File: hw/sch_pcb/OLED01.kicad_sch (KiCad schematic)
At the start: 45 parts, among them J1 Conn_01x04_Male, J2 HEADER_2x03_PARALLEL, J3 HEADER_2x03_PARALLEL, J4 HEADER_2x03_PARALLEL, J5 HEADER_1x03, J6 HEADER_2x05_PARALLEL, U1 TLV840, U2 MIC5504-2.5YM5, U3 MAX5026, U4 TSC2007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

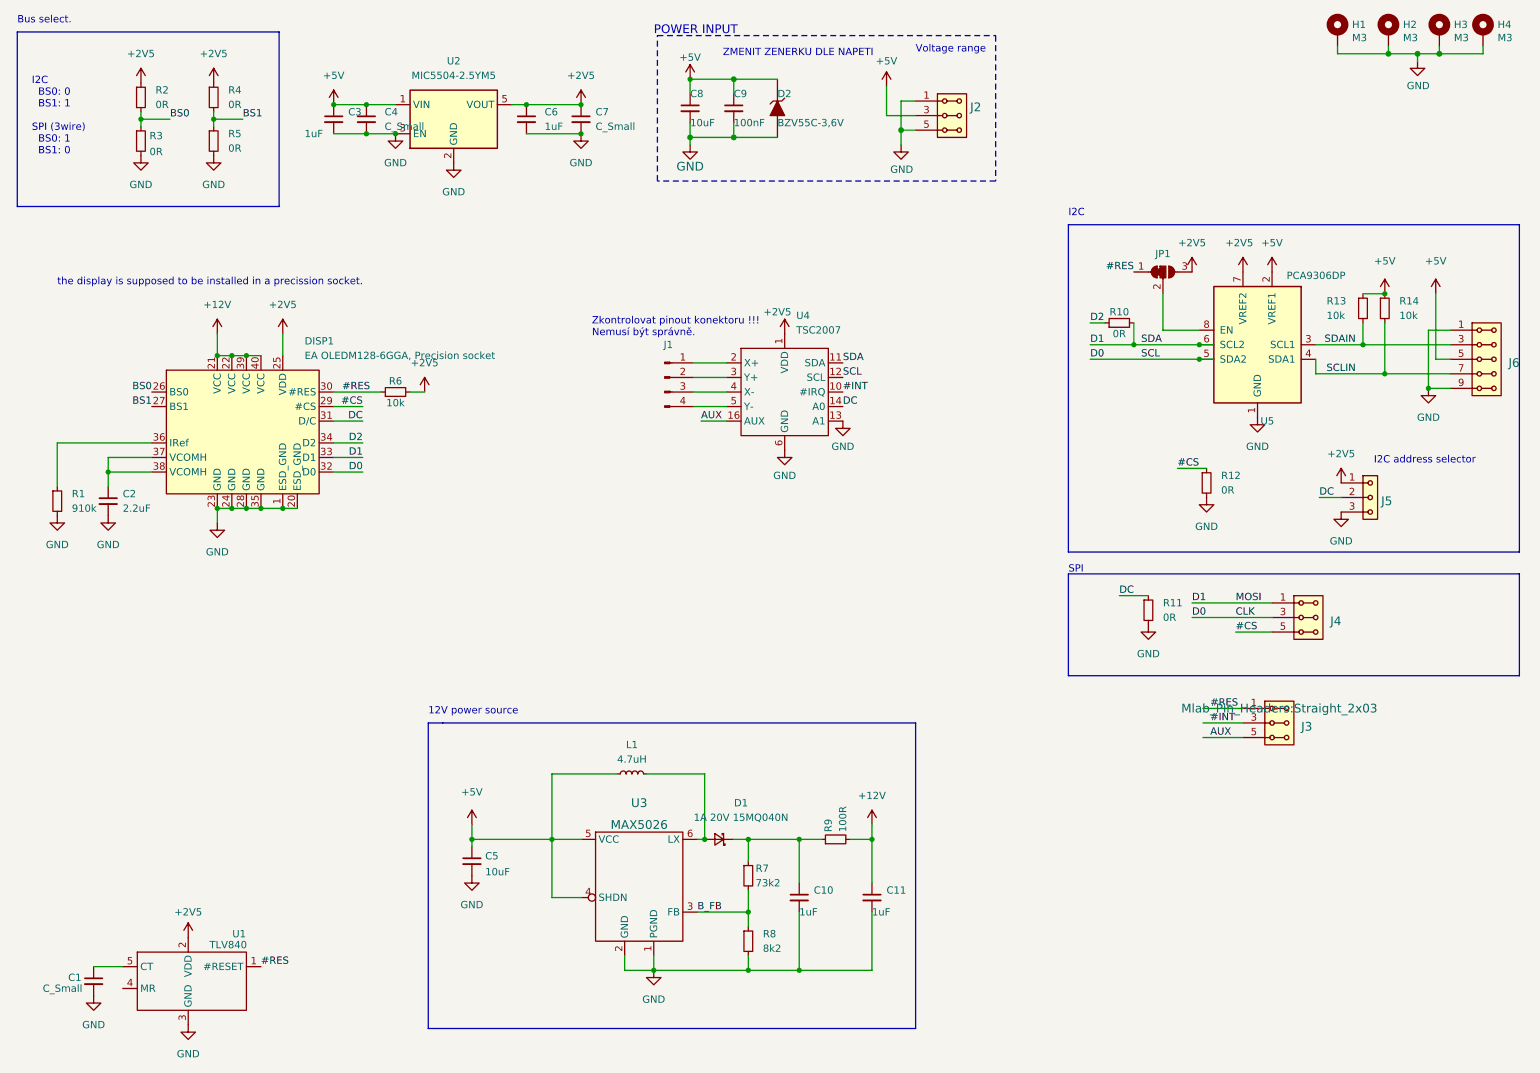
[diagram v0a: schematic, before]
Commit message: Update schematics, add reset circuit, route pcb
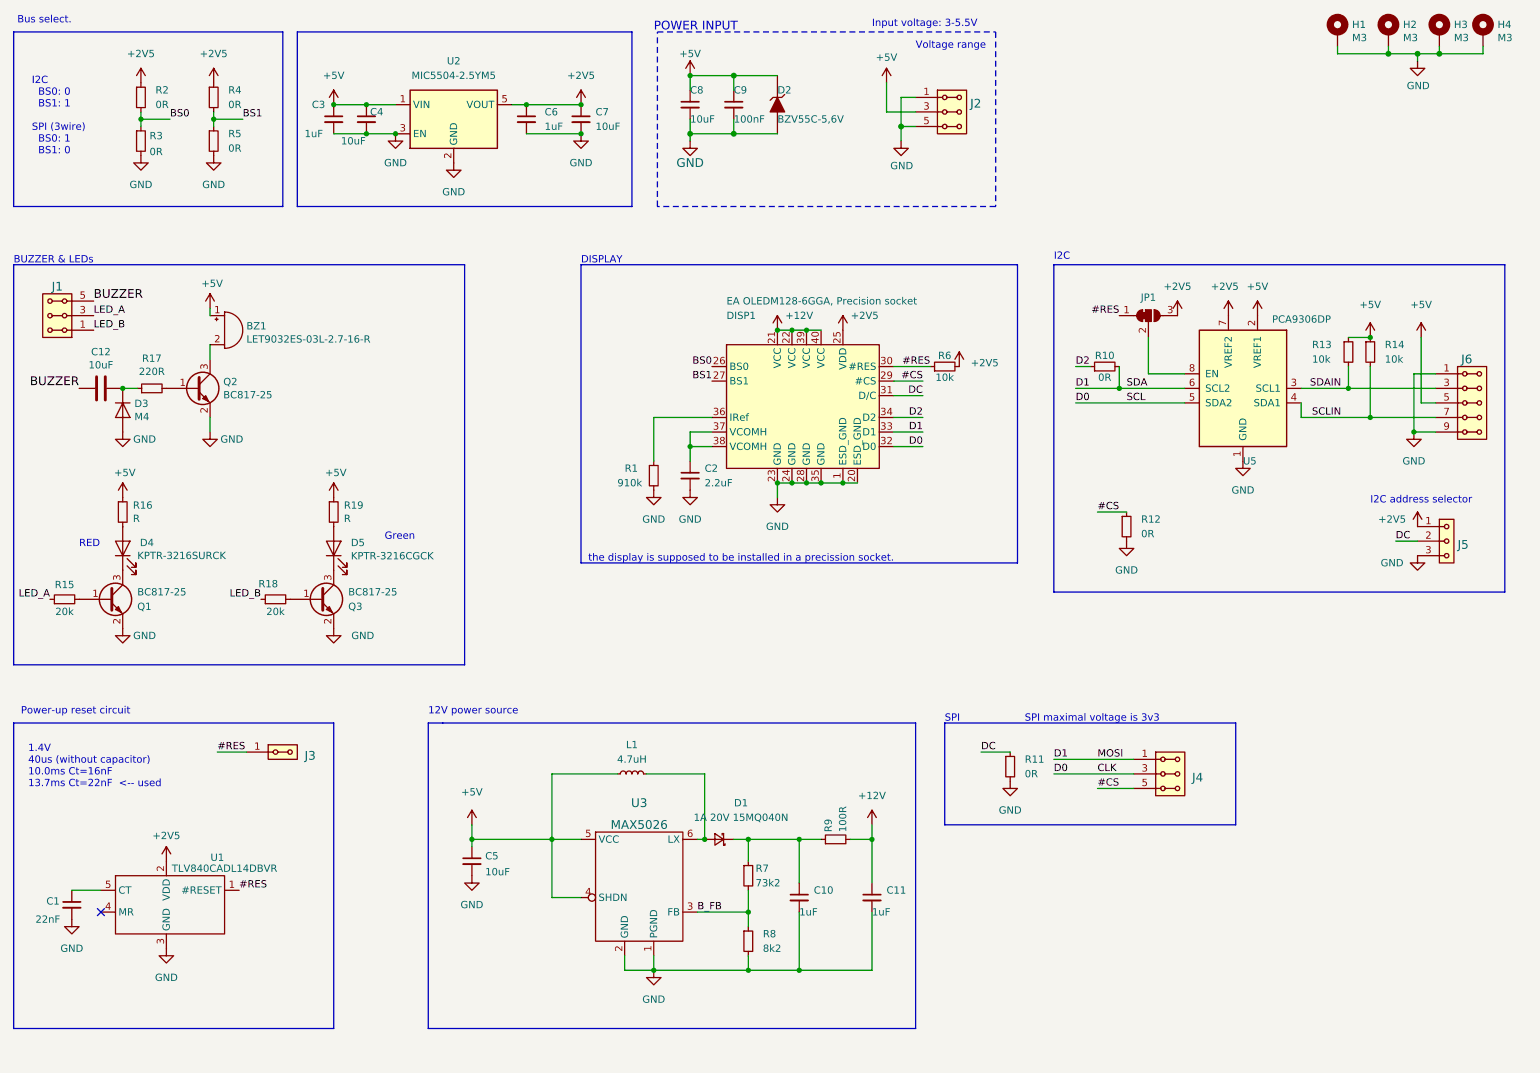
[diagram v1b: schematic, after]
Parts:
- removed J1: Conn_01x04_Male, Connector_FFC-FPC:TE_84952-4_1x04-1MP_P1.0mm_Horizontal, symbol Connector:Conn_01x04_Male
- removed U4: TSC2007, Package_SO:TSSOP-16_4.4x5mm_P0.65mm, symbol MLAB_IO:TSC2007
- added BZ1: LET9032ES-03L-2.7-16-R, MLAB_BUZZER:MagneticBuzzer_LET9032ES-03L-2.7-16-R, symbol Device:Buzzer
- added C12: 10uF, Resistor_SMD:R_0805_2012Metric, symbol Device:C
- added D3: M4, Diode_SMD:D_SMA, symbol Device:D
- added D4: KPTR-3216SURCK, Mlab_D:LED_1206_2, symbol Device:LED
- added D5: KPTR-3216CGCK, Mlab_D:LED_1206_2, symbol Device:LED
- added J1: HEADER_2x03_PARALLEL, Mlab_Pin_Headers:Straight_2x03, symbol MLAB_HEADER:HEADER_2x03_PARALLEL
- added Q1, Q2, Q3: BC817-25, Package_TO_SOT_SMD:SOT-23, symbol Device:Q_NPN_BEC
- added R15, R18: 20k, Resistor_SMD:R_0805_2012Metric, symbol Device:R_Small
- added R16, R19: R, Resistor_SMD:R_0805_2012Metric, symbol Device:R_Small
- added R17: 220R, Resistor_SMD:R_0805_2012Metric, symbol Device:R_Small
- C1: UST_ID (none) -> 5c70984712875079b91f8b4a
- D2: value BZV55C-3,6V -> BZV55C-5,6V; UST_ID (none) -> 5c70984512875079b91f88b2
- J3: value HEADER_2x03_PARALLEL -> HEADER_2x01_PARALLEL; footprint Mlab_Pin_Headers:Straight_2x03 -> Mlab_Pin_Headers:Straight_2x01; symbol MLAB_HEADER:HEADER_2x03_PARALLEL -> MLAB_HEADER:HEADER_2x01_PARALLEL
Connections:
- net +5V: now also BZ1.1 (-), R16.1, R19.1
- net GND: now also D3.2 (A), Q1.2 (E), Q2.2 (E), Q3.2 (E)
- removed net #INT: J3.3, J3.4
- removed net AUX: J3.5, J3.6
- new net: D5.2 (A), R19.2
- new net: C12.2, D3.1 (K), R17.1
- new net: D4.1 (K), Q1.3 (C)
- new net: D4.2 (A), R16.2
- new net: Q1.1 (B), R15.2
- new net: Q3.1 (B), R18.2
- new net: D5.1 (K), Q3.3 (C)
- new net: Q2.1 (B), R17.2
- new net: BZ1.2 (+), Q2.3 (C)
- new net BUZZER: C12.1, J1.5, J1.6
- new net LED_A: J1.3, J1.4, R15.1
- new net LED_B: J1.1, J1.2, R18.1
- no-connect marks 0 -> 1
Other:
- note added: "1.4V 40us (without capacitor) 10.0ms Ct=16nF 13.7ms Ct=22nF <-- used"
- note added: "BUZZER & LEDs"
- note added: "DISPLAY"
- note added: "Green"
- note added: "Input voltage: 3-5.5V"
- note added: "Power-up reset circuit"
- note added: "RED"
- note added: "SPI maximal voltage is 3v3"
- note removed: "ZMENIT ZENERKU DLE NAPETI"
- note removed: "Zkontrolovat pinout konektoru !!! Nemusí být správně."
- moved on the sheet: C1, C2, C8, C9, D2, DISP1, J2, J4, J5, J6, JP1, R1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

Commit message: update assets
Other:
- note added: "Or CMI-9653S-SMT-TR with integrated driver (replace C12 with jumper, remove D3)"
- moved on the sheet: L1
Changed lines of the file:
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@@
     (stroke (width 0) (type default) (color 0 0 0 0))
   )
-  (wire (pts (xy 139.7 148.59) (xy 139.7 160.02))
+  (wire (pts (xy 139.7 151.13) (xy 139.7 160.02))
     (stroke (width 0) (type default) (color 0 0 0 0))
   )
@@
     (stroke (width 0) (type default) (color 0 0 0 0))
   )
-  (wire (pts (xy 129.54 148.59) (xy 139.7 148.59))
+  (wire (pts (xy 129.54 151.13) (xy 139.7 151.13))
     (stroke (width 0) (type default) (color 0 0 0 0))
   )
@@
     (stroke (width 0) (type solid) (color 0 0 0 0))
   )
-  (wire (pts (xy 124.46 148.59) (xy 113.03 148.59))
+  (wire (pts (xy 124.46 151.13) (xy 113.03 151.13))
     (stroke (width 0) (type default) (color 0 0 0 0))
   )
@@
     (stroke (width 0) (type default) (color 0 0 0 0))
   )
-  (wire (pts (xy 113.03 148.59) (xy 113.03 160.02))
+  (wire (pts (xy 113.03 151.13) (xy 113.03 160.02))
     (stroke (width 0) (type default) (color 0 0 0 0))
   )
@@
   )
   (text "12V power source" (at 91.44 138.43 0)
+    (effects (font (size 1.27 1.27)) (justify left bottom))
+  )
+  (text "Or CMI-9653S-SMT-TR\nwith integrated driver\n(replace C12 with jumper, remove D3)"
+    (at 59.69 67.31 0)
     (effects (font (size 1.27 1.27)) (justify left bottom))
   )
@@
     (pin "1")
   )
-  (symbol (lib_id "Device:L_Small") (at 127 148.59 90) (unit 1)
-    (in_bom yes) (on_board yes) (fields_autoplaced)
-    (property "Reference" "L1" (id 0) (at 127 143.51 90))
-    (property "Value" "4.7uH" (id 1) (at 127 146.05 90))
-    (property "Footprint" "Inductor_SMD:L_Bourns_SRN6045TA" (id 2) (at 127 148.59 0)
-      (effects (font (size 1.27 1.27)) hide)
-    )
-    (property "Datasheet" "" (id 3) (at 127 148.59 0)
-      (effects (font (size 1.27 1.27)) hide)
-    )
-    (property "Datasheet" "~" (id 4) (at 127 148.59 0)
-      (effects (font (size 1.27 1.27)) hide)
-    )
-    (property "UST_ID" "5c70984412875079b91f8828" (id 6) (at 127 148.59 90)
+  (symbol (lib_id "Device:L_Small") (at 127 151.13 90) (unit 1)
+    (in_bom yes) (on_board yes) (fields_autoplaced)
+    (property "Reference" "L1" (id 0) (at 127 146.05 90))
+    (property "Value" "4.7uH" (id 1) (at 127 148.59 90))
+    (property "Footprint" "Inductor_SMD:L_Bourns_SRN6045TA" (id 2) (at 127 151.13 0)
+      (effects (font (size 1.27 1.27)) hide)
+    )
+    (property "Datasheet" "" (id 3) (at 127 151.13 0)
+      (effects (font (size 1.27 1.27)) hide)
+    )
+    (property "Datasheet" "~" (id 4) (at 127 151.13 0)
+      (effects (font (size 1.27 1.27)) hide)
+    )
+    (property "UST_ID" "5c70984412875079b91f8828" (id 6) (at 127 151.13 90)
       (effects (font (size 1.27 1.27)) hide)
     )
@@
   )
   (symbol (lib_id "MLAB_IO:MAX5026") (at 128.27 167.64 0) (unit 1)
-    (in_bom yes) (on_board yes) (fields_autoplaced)
-    (property "Reference" "U3" (id 0) (at 128.27 153.67 0)
+    (in_bom yes) (on_board yes)
+    (property "Reference" "U3" (id 0) (at 128.27 154.94 0)
       (effects (font (size 1.524 1.524)))
     )

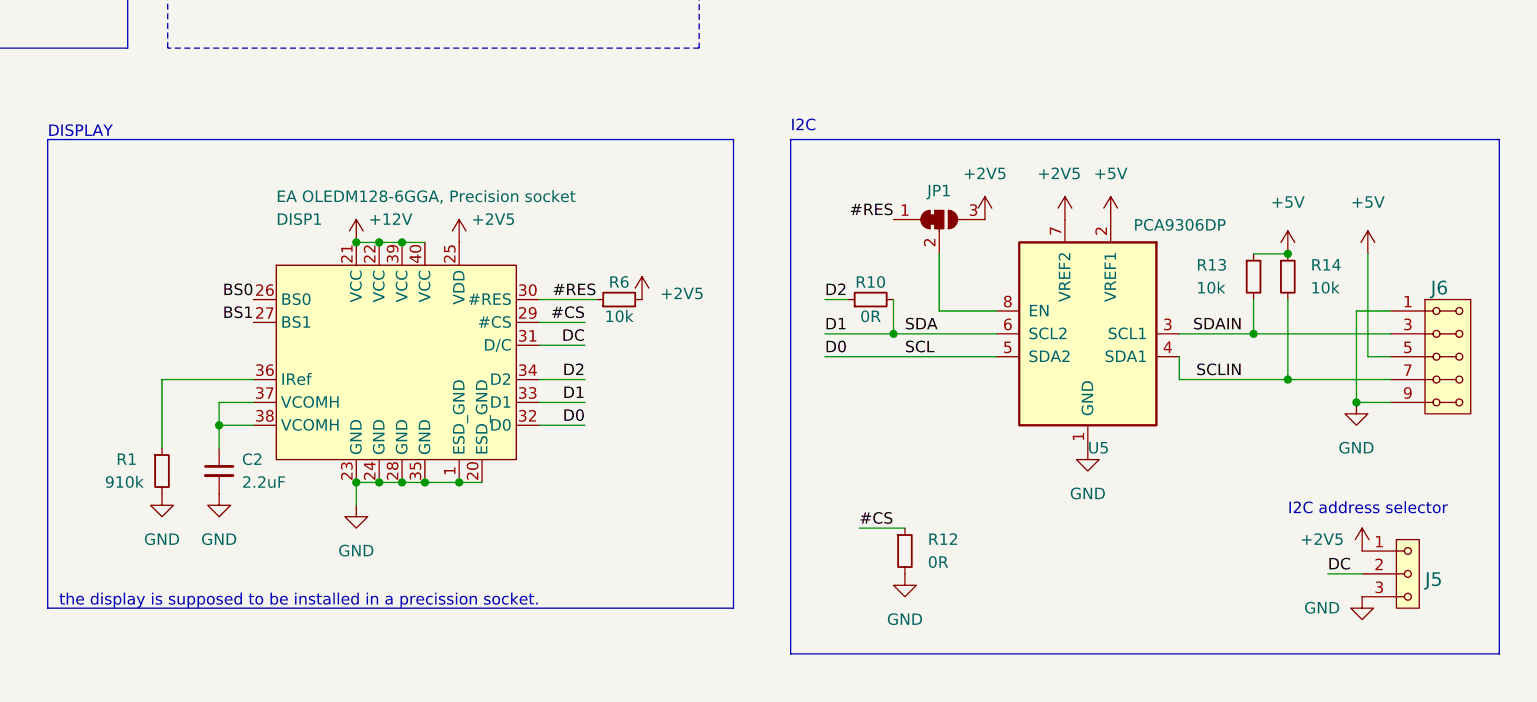
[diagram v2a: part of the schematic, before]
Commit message: i2c level convertor
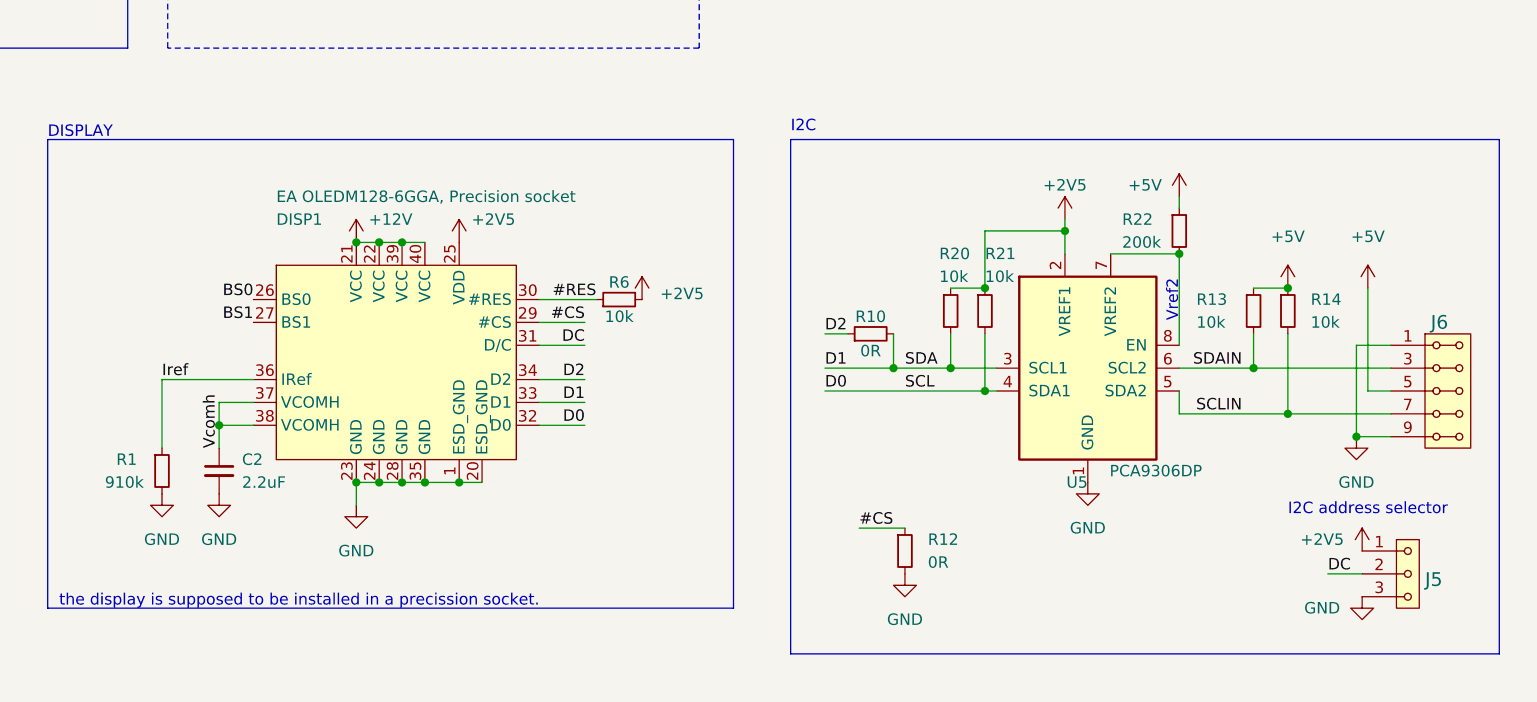
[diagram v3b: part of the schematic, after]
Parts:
- removed JP1: SolderJumper_3_Bridged12, Jumper:SolderJumper-3_P1.3mm_Bridged12_RoundedPad1.0x1.5mm, symbol Jumper:SolderJumper_3_Bridged12
- added R20, R21: 10k, Resistor_SMD:R_0805_2012Metric, symbol Device:R_Small
- added R22: 200k, Resistor_SMD:R_0805_2012Metric, symbol Device:R_Small
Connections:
- net +2V5: now also U5.2 (VREF1), R20.1, R21.1; no longer U5.7 (VREF2)
- net +5V: now also R22.1; no longer U5.2 (VREF1)
- net CLK: now also U5.4 (SDA1), R21.2; no longer U5.5 (SDA2)
- net D1: now also U5.3 (SCL1), R20.2; no longer U5.6 (SCL2)
- net SCLIN: now also U5.5 (SDA2); no longer U5.4 (SDA1)
- net SDAIN: now also U5.6 (SCL2); no longer U5.3 (SCL1)
- net at U5.8 (EN): now also U5.7 (VREF2), R22.2
- net Vcomh: now reaches C2.1, DISP1.37 (VCOMH), DISP1.38 (VCOMH)
- net Iref: now reaches DISP1.36 (IRef), R1.1
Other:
- note added: "Vref2"
- moved on the sheet: J6, R10, R13, R14, U5

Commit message: update schematics, layout, improve silkscreen
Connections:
- net CLK: now also R20.2, U5.3 (SCL1); no longer R21.2, U5.4 (SDA1)
- net D1: now also R21.2, U5.4 (SDA1); no longer R20.2, U5.3 (SCL1)
- net SCLIN: now also J6.3, J6.4, R13.2, U5.6 (SCL2); no longer J6.7, J6.8, R14.2, U5.5 (SDA2)
- net SDAIN: now also J6.7, J6.8, R14.2, U5.5 (SDA2); no longer J6.3, J6.4, R13.2, U5.6 (SCL2)
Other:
- moved on the sheet: J6, R10, R14

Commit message: solve DRC
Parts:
- removed J4: HEADER_2x03_PARALLEL, Mlab_Pin_Headers:Straight_2x03, symbol MLAB_HEADER:HEADER_2x03_PARALLEL
- removed R10, R11, R12, R2, R4, R5: 0R, Resistor_SMD:R_0805_2012Metric, symbol Device:R_Small
- added J4: Conn_01x04_Shielded, Mlab_CON:EA_WF100-04S, symbol Connector_Generic_Shielded:Conn_01x04_Shielded
- added U4: TSC2007IPWG4, Mlab_IO:SOP65P640X120-16N, symbol MLAB_IO:TSC2007IPWG4
- J3: footprint Mlab_Pin_Headers:Straight_2x01 -> Mlab_Pin_Headers:Straight_2x02; symbol MLAB_HEADER:HEADER_2x01_PARALLEL -> MLAB_HEADER:HEADER_2x02_PARALLEL
- R3: value 0R -> 33R; UST_ID 5c70984512875079b91f896b -> (none)
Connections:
- net #CS is gone; now on net GND: DISP1.29 (#CS)
- net BS1 is gone; now on net +2V5: DISP1.27 (BS1)
- net D2 is gone; now on net D1: DISP1.34 (D2)
- net +2V5: now also U4.1 (VDD/REF)
- net D1: now also U4.11 (SDA)
- net GND: now also DISP1.26 (BS0), J4.SH (Shield), U4.6 (GND); no longer R3.2
- net BS0: no longer names the net of R3.1
- net BS0: now also U4.10 (~{PENIRQ}); no longer DISP1.26 (BS0)
- net CLK renamed D0
- net D0: now also U4.12 (SCL)
- net DC renamed ADDR
- net ADDR: now also U4.14 (A0)
- new net #INT: J3.3, J3.4, R3.2
- new net X+: J4.1 (Pin_1), U4.2 (X+)
- new net X-: J4.3 (Pin_3), U4.4 (X-)
- new net Y+: J4.2 (Pin_2), U4.3 (Y+)
- new net Y-: J4.4 (Pin_4), U4.5 (Y-)
- no-connect marks 1 -> 7
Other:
- note removed: "SPI"
- note removed: "SPI maximal voltage is 3v3"
- moved on the sheet: J5, J6, R13, R14, R20, R21, R22, U5

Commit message: Update project and workflow to KiCADv8. Improvements in the PCB layout. Documentation update.
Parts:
- C1: footprint (none) -> Capacitor_SMD:C_0805_2012Metric
- R19: value R -> R
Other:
- title: OLED01A -> OLED01B
- moved on the sheet: C1
